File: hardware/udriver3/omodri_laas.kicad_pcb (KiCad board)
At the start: 2 copper layers, 251 parts, among them J1 Conn_01x12, J10 Conn_01x02, J11 Conn_02x04_Odd_Even, J12 Conn_01x07, J13 Conn_01x07, J2 Conn_01x05, J3 Conn_01x03, J4 Conn_01x02, J5 Conn_01x03, J6 Conn_01x03, J7 Conn_01x03, J8 Conn_01x05, J9 Conn_01x05, Q1 CSD88599Q5DC, Q2 CSD88599Q5DC, Q3 CSD88599Q5DC, Q4 CSD88599Q5DC, Q5 CSD88599Q5DC, Q6 CSD88599Q5DC, SW1 B3U-3100P, U1 DRV8353S, U10 TCAN332G, U11 TPS3703, U12 TPS3703, U13 TPD6E05U06, U14 DSLVDS1048, U15 TPD2E001, U16 TPD2E001, U17 TPD2E001, U18 TPD2E001, U19 TPD6E05U06, U2 DRV8353S, U20 DSLVDS1047, U3 MAX17502FxTB, U4 TMS320F28388D, U5 MPM3804GG, U6 MPM3804GG, U7 REF6230, U8 OPA388, U9 TXB0106, X1 ECS-TXO-2016-33-200-TR

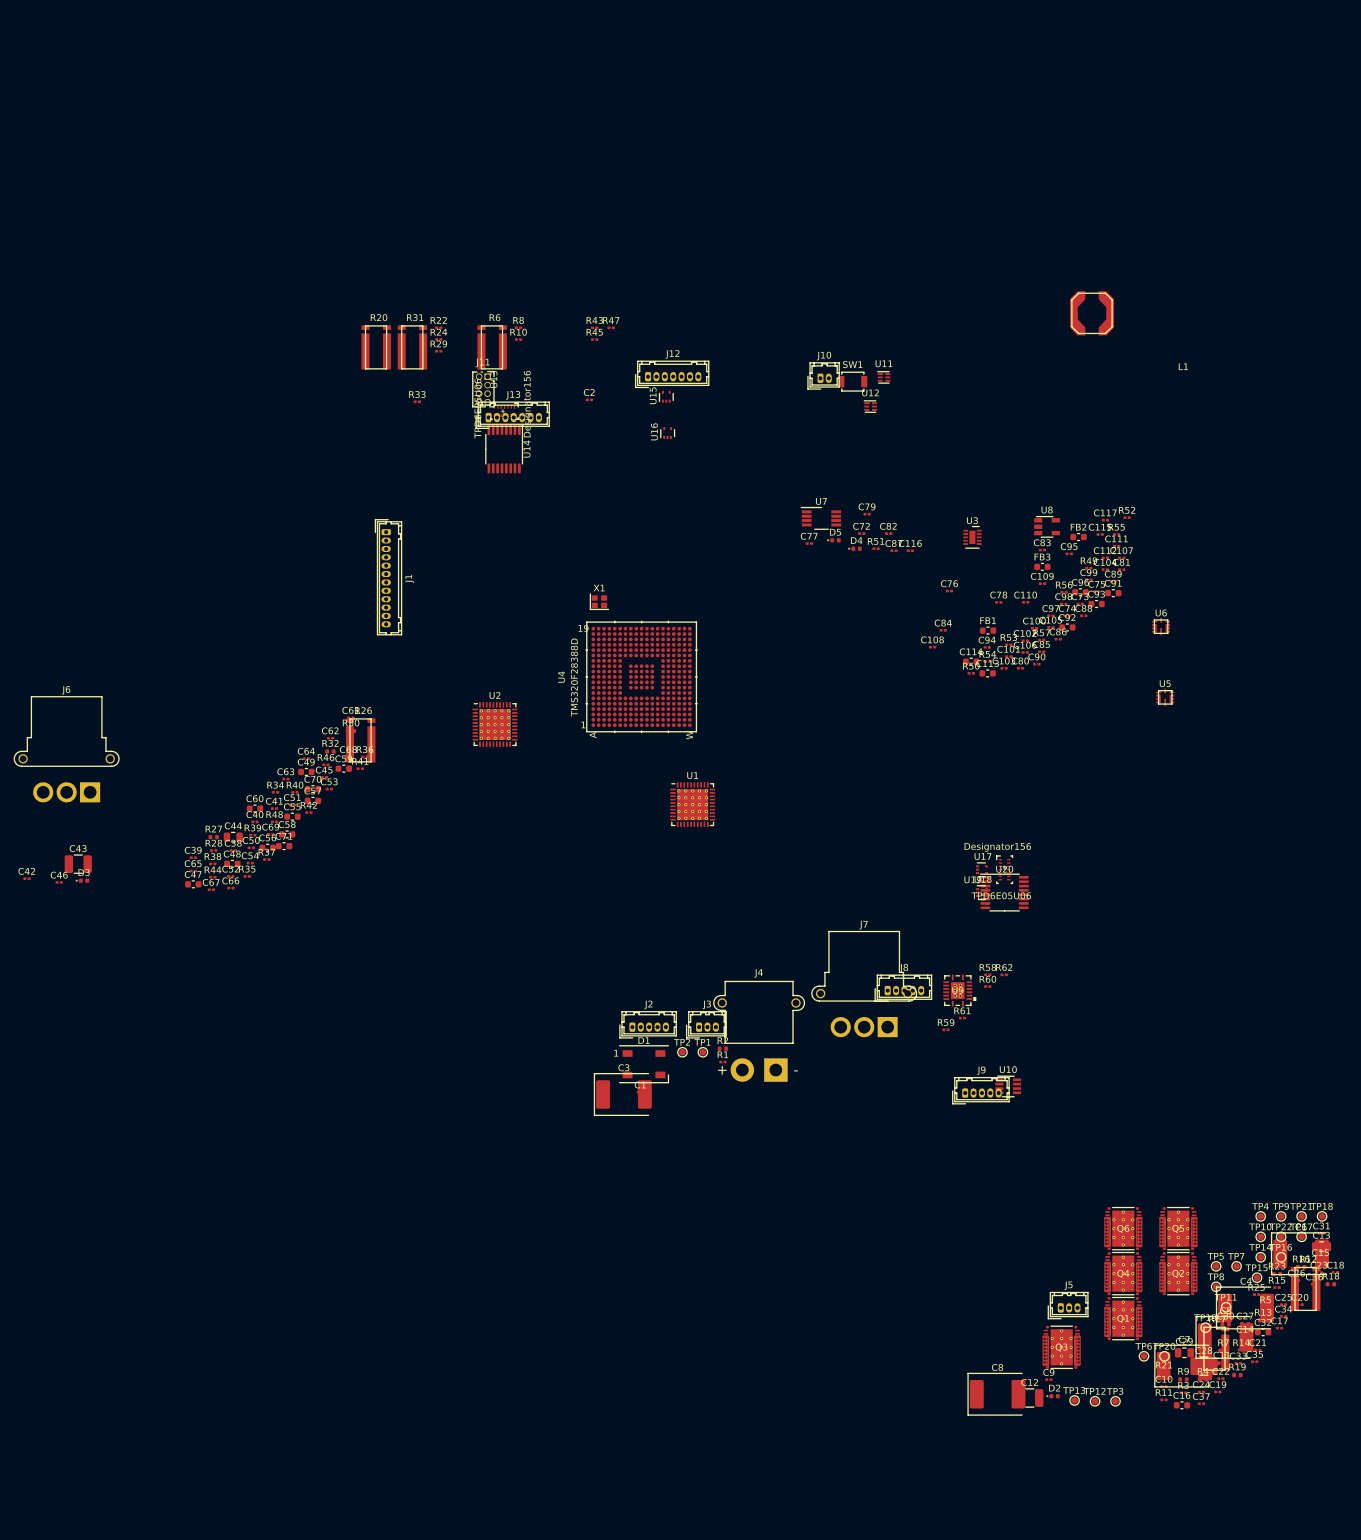
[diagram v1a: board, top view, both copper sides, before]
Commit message: Update of the schematics. Driver and power files split. Placement starting.
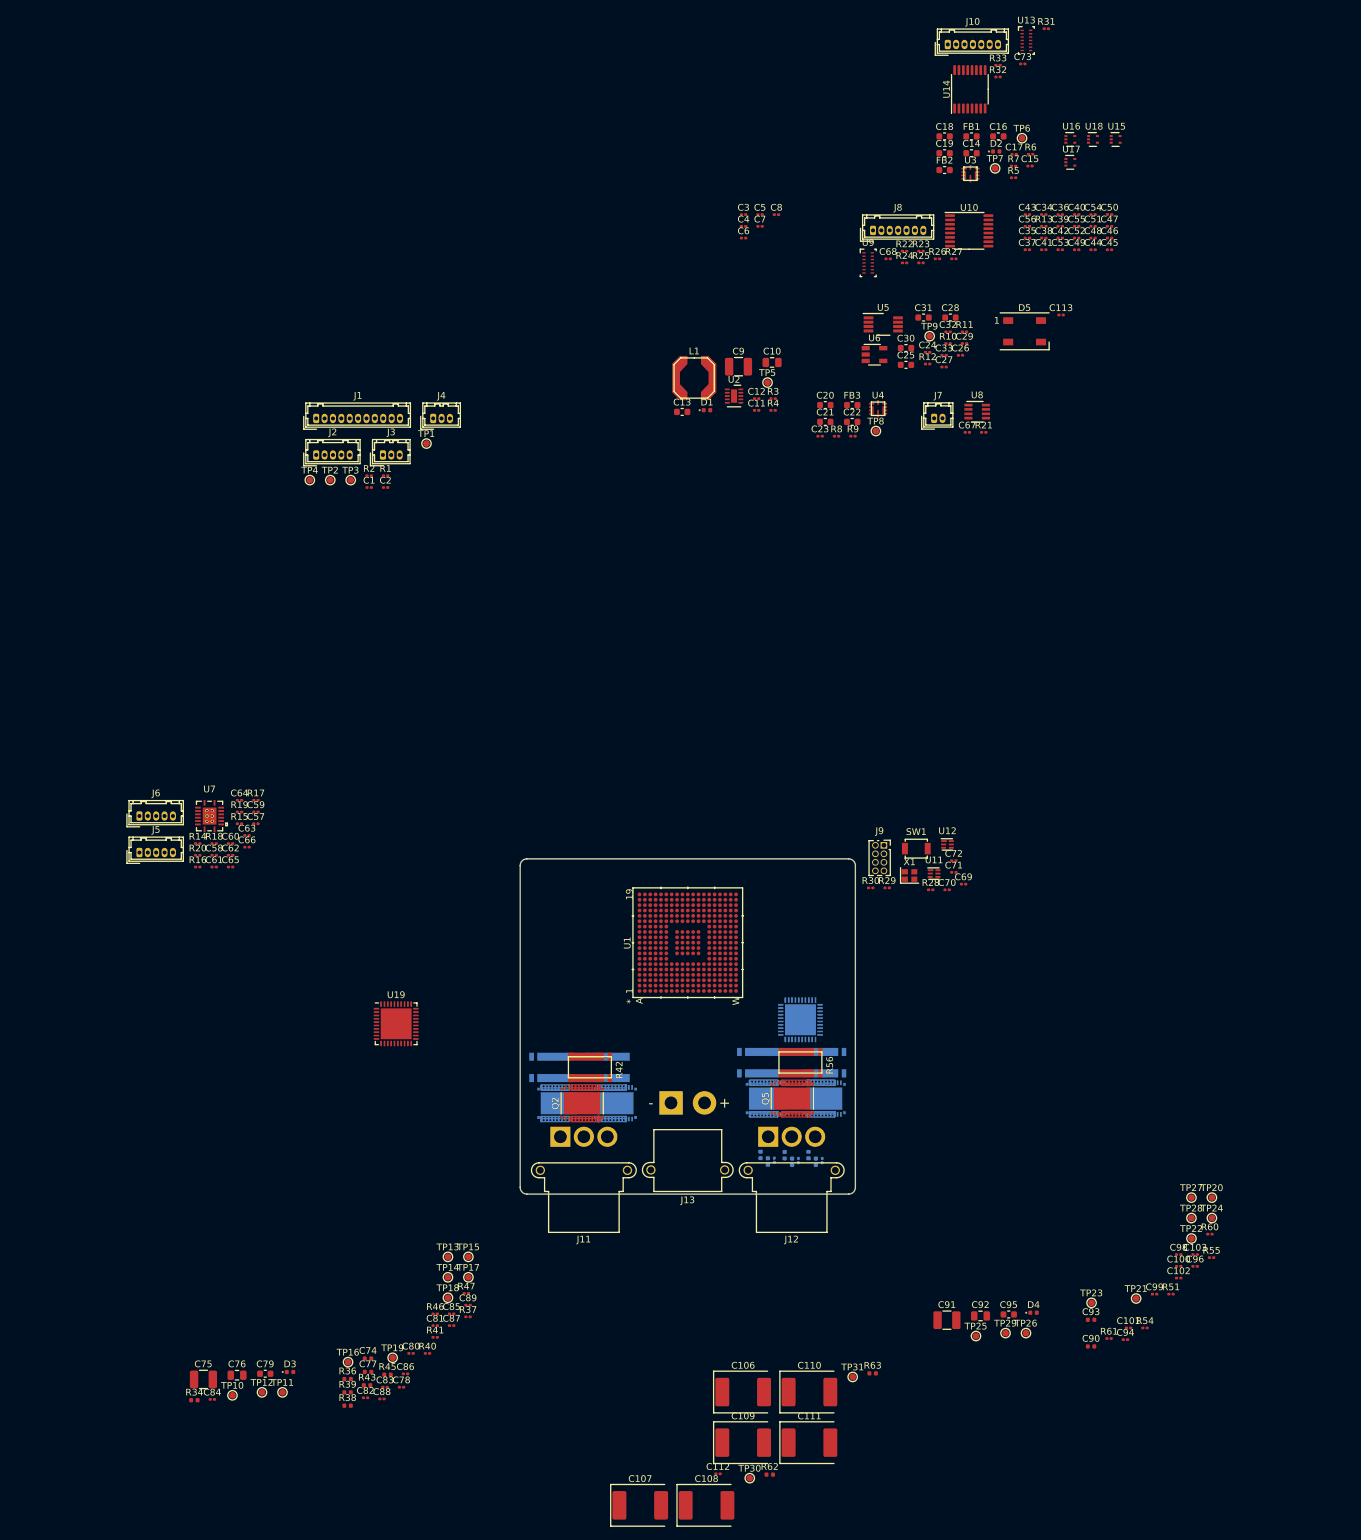
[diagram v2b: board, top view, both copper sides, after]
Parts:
- removed C114: 10uF, Capacitor_SMD:C_0603_1608Metric
- removed C115, C116, C117: 100nF, Capacitor_SMD:C_0201_0603Metric
- added R63: 5.1k, Resistor_SMD:R_0402_1005Metric, F.Cu at (152.6, 126.7)
- added TP23: TestPoint, TestPoint:TestPoint_Pad_D1.0mm, F.Cu at (185.2, 116.2)
- added TP24: TestPoint, TestPoint:TestPoint_Pad_D1.0mm, F.Cu at (203.2, 103.6)
- added TP25: TestPoint, TestPoint:TestPoint_Pad_D1.0mm, F.Cu at (168.0, 121.2)
- added TP26: TestPoint, TestPoint:TestPoint_Pad_D1.0mm, F.Cu at (175.4, 120.7)
- added TP27: TestPoint, TestPoint:TestPoint_Pad_D1.0mm, F.Cu at (200.1, 100.5)
- added TP28: TestPoint, TestPoint:TestPoint_Pad_D1.0mm, F.Cu at (200.1, 103.6)
- added TP29: TestPoint, TestPoint:TestPoint_Pad_D1.0mm, F.Cu at (172.4, 120.7)
- added TP30: TestPoint, TestPoint:TestPoint_Pad_D1.0mm, F.Cu at (134.2, 142.4)
- added TP31: TestPoint, TestPoint:TestPoint_Pad_D1.0mm, F.Cu at (149.6, 127.3)
- C1, C101, C112, C81, C83, C84, C85: value 100nF -> 10nF
- C10: value 10nF -> 100nF; footprint Capacitor_SMD:C_0201_0603Metric -> Capacitor_SMD:C_0805_2012Metric
- C100, C88, C89: value 1uF -> 10nF
- C102, C63, C64, C65, C80, C86: value 100nF -> 1nF
- C104, C105, C97: value 1nF -> 10nF; moved to B.Cu
- C106: value 1uF -> 100uF; footprint Capacitor_SMD:C_0201_0603Metric -> Capacitor_Tantalum_SMD:CP_EIA-7360-38_Kemet-E
- C107, C108, C109, C111: value 100nF -> 100uF; footprint Capacitor_SMD:C_0201_0603Metric -> Capacitor_Tantalum_SMD:CP_EIA-7360-38_Kemet-E
- C11: value 1uF -> 10nF; footprint Capacitor_SMD:C_0402_1005Metric -> Capacitor_SMD:C_0201_0603Metric
- C110: value 10nF -> 100uF; footprint Capacitor_SMD:C_0201_0603Metric -> Capacitor_Tantalum_SMD:CP_EIA-7360-38_Kemet-E
- C113, C47, C48, C49, C55, C56, C70: value 10uF -> 100nF; footprint Capacitor_SMD:C_0603_1608Metric -> Capacitor_SMD:C_0201_0603Metric
- C12: value 10uF -> 1uF; footprint Capacitor_SMD:C_1210_3225Metric -> Capacitor_SMD:C_0201_0603Metric
- C13: value 100nF -> 22uF; footprint Capacitor_SMD:C_0805_2012Metric -> Capacitor_SMD:C_0603_1608Metric
- C14, C30: value 1uF -> 10uF; footprint Capacitor_SMD:C_0402_1005Metric -> Capacitor_SMD:C_0603_1608Metric
- C16: value 47nF -> 10uF
- C17, C23: value 1nF -> 1uF
- C18, C20, C22: value 10nF -> 10uF; footprint Capacitor_SMD:C_0201_0603Metric -> Capacitor_SMD:C_0603_1608Metric
- C19: value 100nF -> 22uF; footprint Capacitor_SMD:C_0201_0603Metric -> Capacitor_SMD:C_0603_1608Metric
- C21: value 10nF -> 22uF; footprint Capacitor_SMD:C_0201_0603Metric -> Capacitor_SMD:C_0603_1608Metric
- C24, C26, C34, C36, C37, C38, C40, C42, C45: value 10nF -> 100nF
- C25: value 1nF -> 10uF; footprint Capacitor_SMD:C_0201_0603Metric -> Capacitor_SMD:C_0603_1608Metric
- C27: footprint Capacitor_SMD:C_0402_1005Metric -> Capacitor_SMD:C_0201_0603Metric
- C28: footprint Capacitor_SMD:C_1210_3225Metric -> Capacitor_SMD:C_0603_1608Metric
- C29: value 100nF -> 1uF; footprint Capacitor_SMD:C_0805_2012Metric -> Capacitor_SMD:C_0201_0603Metric
- C3, C4, C5, C6, C7, C8: value 100uF -> 100nF; footprint Capacitor_Tantalum_SMD:CP_EIA-7360-38_Kemet-E -> Capacitor_SMD:C_0201_0603Metric
- C31: value 1uF -> 10uF; footprint Capacitor_SMD:C_0201_0603Metric -> Capacitor_SMD:C_0603_1608Metric
- C32: value 47nF -> 100nF; footprint Capacitor_SMD:C_0603_1608Metric -> Capacitor_SMD:C_0201_0603Metric
- C33, C39, C41, C98: value 1nF -> 100nF
- C43: value 10uF -> 100nF; footprint Capacitor_SMD:C_1210_3225Metric -> Capacitor_SMD:C_0201_0603Metric
- C44: footprint Capacitor_SMD:C_0805_2012Metric -> Capacitor_SMD:C_0201_0603Metric
- C46, C51, C53, C67, C68, C69: value 1uF -> 100nF
- C57, C58, C59, C96: value 10uF -> 1nF; footprint Capacitor_SMD:C_0603_1608Metric -> Capacitor_SMD:C_0201_0603Metric
- C60: value 10uF -> 1uF; footprint Capacitor_SMD:C_0603_1608Metric -> Capacitor_SMD:C_0201_0603Metric
- C66, C78, C94: value 100nF -> 1uF
- C71: value 10uF -> 10nF; footprint Capacitor_SMD:C_0603_1608Metric -> Capacitor_SMD:C_0201_0603Metric
- C74, C77: value 100nF -> 1uF; footprint Capacitor_SMD:C_0201_0603Metric -> Capacitor_SMD:C_0402_1005Metric
- C75: value 100nF -> 10uF; footprint Capacitor_SMD:C_0201_0603Metric -> Capacitor_SMD:C_1210_3225Metric
- C76: footprint Capacitor_SMD:C_0201_0603Metric -> Capacitor_SMD:C_0805_2012Metric
- C79: value 100nF -> 47nF; footprint Capacitor_SMD:C_0201_0603Metric -> Capacitor_SMD:C_0603_1608Metric
- C87: value 1uF -> 1nF
- C9: value 10nF -> 10uF; footprint Capacitor_SMD:C_0201_0603Metric -> Capacitor_SMD:C_1210_3225Metric
- C90: footprint Capacitor_SMD:C_0201_0603Metric -> Capacitor_SMD:C_0402_1005Metric
- C91: footprint Capacitor_SMD:C_0603_1608Metric -> Capacitor_SMD:C_1210_3225Metric
- C92: value 10uF -> 100nF; footprint Capacitor_SMD:C_0603_1608Metric -> Capacitor_SMD:C_0805_2012Metric
- C93: value 10uF -> 1uF; footprint Capacitor_SMD:C_0603_1608Metric -> Capacitor_SMD:C_0402_1005Metric
- C95: value 1uF -> 47nF; footprint Capacitor_SMD:C_0201_0603Metric -> Capacitor_SMD:C_0603_1608Metric
- C99: value 1nF -> 10nF
- D1: value WS2812B -> LED GREEN; footprint LED_SMD:LED_WS2812B_PLCC4_5.0x5.0mm_P3.2mm -> LED_SMD:LED_0402_1005Metric
- D2: value LED RED -> LED GREEN
- D4: value LED GREEN -> LED RED
- D5: value LED GREEN -> WS2812B; footprint LED_SMD:LED_0402_1005Metric -> LED_SMD:LED_WS2812B_PLCC4_5.0x5.0mm_P3.2mm
- FB1, FB2, FB3: value Ferrite_Bead_Small -> 220R@100MHz
- J1: value Conn_01x12 -> Conn_01x11; footprint Connector_Hirose:Hirose_DF13-12P-1.25DSA_1x12_P1.25mm_Vertical -> Connector_Hirose:Hirose_DF13-11P-1.25DSA_1x11_P1.25mm_Vertical
- J10: value Conn_01x02 -> Conn_01x07; footprint Connector_Hirose:Hirose_DF13-02P-1.25DSA_1x02_P1.25mm_Vertical -> Connector_Hirose:Hirose_DF13-07P-1.25DSA_1x07_P1.25mm_Vertical
- J11: value Conn_02x04_Odd_Even -> Conn_01x03; footprint Connector_PinSocket_1.27mm:PinSocket_2x04_P1.27mm_Vertical -> Connector_AMASS:AMASS_MR30PW-FB_1x03_P3.50mm_Horizontal
- J12: value Conn_01x07 -> Conn_01x03; footprint Connector_Hirose:Hirose_DF13-07P-1.25DSA_1x07_P1.25mm_Vertical -> Connector_AMASS:AMASS_MR30PW-FB_1x03_P3.50mm_Horizontal
- J13: value Conn_01x07 -> Conn_01x02; footprint Connector_Hirose:Hirose_DF13-07P-1.25DSA_1x07_P1.25mm_Vertical -> Connector_AMASS:AMASS_XT30PW-M_1x02_P2.50mm_Horizontal
- J4: value Conn_01x02 -> Conn_01x03; footprint Connector_AMASS:AMASS_XT30PW-M_1x02_P2.50mm_Horizontal -> Connector_Hirose:Hirose_DF13-03P-1.25DSA_1x03_P1.25mm_Vertical
- J5: value Conn_01x03 -> Conn_01x05; footprint Connector_Hirose:Hirose_DF13-03P-1.25DSA_1x03_P1.25mm_Vertical -> Connector_Hirose:Hirose_DF13-05P-1.25DSA_1x05_P1.25mm_Vertical
- J6: value Conn_01x03 -> Conn_01x05; footprint Connector_AMASS:AMASS_MR30PW-FB_1x03_P3.50mm_Horizontal -> Connector_Hirose:Hirose_DF13-05P-1.25DSA_1x05_P1.25mm_Vertical
- J7: value Conn_01x03 -> Conn_01x02; footprint Connector_AMASS:AMASS_MR30PW-FB_1x03_P3.50mm_Horizontal -> Connector_Hirose:Hirose_DF13-02P-1.25DSA_1x02_P1.25mm_Vertical
- J8: value Conn_01x05 -> Conn_01x07; footprint Connector_Hirose:Hirose_DF13-05P-1.25DSA_1x05_P1.25mm_Vertical -> Connector_Hirose:Hirose_DF13-07P-1.25DSA_1x07_P1.25mm_Vertical
- J9: value Conn_01x05 -> Conn_02x04_Odd_Even; footprint Connector_Hirose:Hirose_DF13-05P-1.25DSA_1x05_P1.25mm_Vertical -> Connector_PinSocket_1.27mm:PinSocket_2x04_P1.27mm_Vertical
- L1: footprint udrive3:L_coilcraft_LPS62xx -> udriver3:L_coilcraft_LPS62xx
- Q1, Q3, Q4, Q6: footprint udrive3:VSON_CLIP_22 -> udriver3:VSON_CLIP_22; moved to B.Cu
- Q2, Q5: footprint udrive3:VSON_CLIP_22 -> udriver3:VSON_CLIP_22
- R10, R11: value 120 -> 0.1
- R12: value 0.005 -> 0.1; footprint udrive3:FC4L64 -> Resistor_SMD:R_0201_0603Metric
- R13: value 5.1k -> 56; footprint Resistor_SMD:R_0402_1005Metric -> Resistor_SMD:R_0201_0603Metric
- R14: value 220 -> 1k
- R15: value 10k -> 1k
- R16, R19, R30: value 100k -> 1k; footprint Resistor_SMD:R_0402_1005Metric -> Resistor_SMD:R_0201_0603Metric
- R17, R20: value 0.005 -> 1k; footprint udrive3:FC4L64 -> Resistor_SMD:R_0201_0603Metric
- R18, R4: value 5.1k -> 1k; footprint Resistor_SMD:R_0402_1005Metric -> Resistor_SMD:R_0201_0603Metric
- R2: value 100k -> 120; footprint Resistor_SMD:R_0402_1005Metric -> Resistor_SMD:R_0201_0603Metric
- R21: value 5.1k -> 120; footprint Resistor_SMD:R_0402_1005Metric -> Resistor_SMD:R_0201_0603Metric
- R22, R24: value 120 -> 100
- R23: value 100k -> 100; footprint Resistor_SMD:R_0402_1005Metric -> Resistor_SMD:R_0201_0603Metric
- R25: value 120 -> 10k
- R26, R31: value 0.005 -> 10k; footprint udrive3:FC4L64 -> Resistor_SMD:R_0201_0603Metric
- R27, R32: value 5.1k -> 10k; footprint Resistor_SMD:R_0402_1005Metric -> Resistor_SMD:R_0201_0603Metric
- R28: value 220 -> 10k
- R3, R8: value 120 -> 100k
- R34: value 470 -> 100k; footprint Resistor_SMD:R_0201_0603Metric -> Resistor_SMD:R_0402_1005Metric
- R35: value 100k -> 0.005; footprint Resistor_SMD:R_0201_0603Metric -> udriver3:FC4L64; moved to B.Cu
- R36: value 22.1k -> 5.1k; footprint Resistor_SMD:R_0201_0603Metric -> Resistor_SMD:R_0402_1005Metric
- R37: value 220 -> 120
- R38, R39: footprint Resistor_SMD:R_0201_0603Metric -> Resistor_SMD:R_0402_1005Metric
- R40: value 56 -> 120
- R41, R51: value 1k -> 120
- R42: value 1k -> 0.005; footprint Resistor_SMD:R_0201_0603Metric -> udriver3:FC4L64
- R43, R45: value 1k -> 5.1k; footprint Resistor_SMD:R_0201_0603Metric -> Resistor_SMD:R_0402_1005Metric
- R44: value 1k -> 0.005; footprint Resistor_SMD:R_0201_0603Metric -> udriver3:FC4L64; moved to B.Cu
- R46: value 1k -> 470
- R47: value 1k -> 10k
- R48: value 120 -> 100k; footprint Resistor_SMD:R_0201_0603Metric -> Resistor_SMD:R_0402_1005Metric; moved to B.Cu
- R49: value 10k -> 0.005; footprint Resistor_SMD:R_0201_0603Metric -> udriver3:FC4L64; moved to B.Cu
- R5, R9: footprint Resistor_SMD:R_0402_1005Metric -> Resistor_SMD:R_0201_0603Metric
- R50, R57: value 10k -> 5.1k; footprint Resistor_SMD:R_0201_0603Metric -> Resistor_SMD:R_0402_1005Metric; moved to B.Cu
- R52, R53: value 100 -> 100k; footprint Resistor_SMD:R_0201_0603Metric -> Resistor_SMD:R_0402_1005Metric; moved to B.Cu
- R54: value 100 -> 120
- R55: value 10k -> 120
- R56: value 10k -> 0.005; footprint Resistor_SMD:R_0201_0603Metric -> udriver3:FC4L64
- R58: value 0.1 -> 0.005; footprint Resistor_SMD:R_0201_0603Metric -> udriver3:FC4L64; moved to B.Cu
- R59: value 0.1 -> 5.1k; footprint Resistor_SMD:R_0201_0603Metric -> Resistor_SMD:R_0402_1005Metric; moved to B.Cu
- R6: value 0.005 -> 22.1k; footprint udrive3:FC4L64 -> Resistor_SMD:R_0201_0603Metric
- R60: value 10k -> 470
- R62: value 10k -> 100k; footprint Resistor_SMD:R_0201_0603Metric -> Resistor_SMD:R_0402_1005Metric
- R7: value 5.1k -> 470; footprint Resistor_SMD:R_0402_1005Metric -> Resistor_SMD:R_0201_0603Metric
- U1: value DRV8353S -> TMS320F28388D; footprint Package_DFN_QFN:QFN-40-1EP_6x6mm_P0.5mm_EP4.6x4.6mm_ThermalVias -> udriver3:NFBGA_337
- U10: value TCAN332G -> DSLVDS1048; footprint Package_TO_SOT_SMD:TSOT-23-8 -> Package_SO:TSSOP-16_4.4x5mm_P0.65mm
- U13: footprint udrive3:USON_14 -> udriver3:USON_14
- U14: value DSLVDS1048 -> DSLVDS1047
- U19: value TPD6E05U06 -> DRV8353S; footprint udrive3:USON_14 -> Package_DFN_QFN:QFN-40-1EP_6x6mm_P0.5mm_EP4.6x4.6mm
- U2: value DRV8353S -> MAX17502FxTB; footprint Package_DFN_QFN:QFN-40-1EP_6x6mm_P0.5mm_EP4.6x4.6mm_ThermalVias -> Package_DFN_QFN:TDFN-10-1EP_2x3mm_P0.5mm_EP0.9x2mm
- U20: value DSLVDS1047 -> DRV8353S; footprint Package_SO:TSSOP-16_4.4x5mm_P0.65mm -> Package_DFN_QFN:QFN-40-1EP_6x6mm_P0.5mm_EP4.6x4.6mm; moved to B.Cu
- U3: value MAX17502FxTB -> MPM3804GG; footprint Package_DFN_QFN:TDFN-10-1EP_2x3mm_P0.5mm_EP0.9x2mm -> udriver3:QFN-10_2x2mm_P0.5mm
- U4: value TMS320F28388D -> MPM3804GG; footprint udrive3:NFBGA_337 -> udriver3:QFN-10_2x2mm_P0.5mm
- U5: value MPM3804GG -> REF6230; footprint udrive3:QFN-10_2x2mm_P0.5mm -> Package_SO:VSSOP-8_3.0x3.0mm_P0.65mm
- U6: value MPM3804GG -> OPA388; footprint udrive3:QFN-10_2x2mm_P0.5mm -> Package_TO_SOT_SMD:TSOT-23-5
- U7: value REF6230 -> TXB0106; footprint Package_SO:VSSOP-8_3.0x3.0mm_P0.65mm -> udriver3:PVQFN_17
- U8: value OPA388 -> TCAN332G; footprint Package_TO_SOT_SMD:TSOT-23-5 -> Package_TO_SOT_SMD:TSOT-23-8
- U9: value TXB0106 -> TPD6E05U06; footprint udrive3:PVQFN_17 -> udriver3:USON_14
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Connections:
- C1 pad 1: VDD_3V3 -> /sheet5F597565/ANALOG_IN2
- C10 pad 1: /F2838x GPIOs/ANALOG_IN1 -> VPOWER
- C100 pad 1: 5V0 -> /sheet5F597565/M2_Ib
- C101 pad 1: VDD_3V3 -> /sheet5F597565/M2_Ia
- C102 pad 1: 5V0 -> /Sheet5F71C92D/SPB
- C102 pad 2: GND -> /Sheet5F71C92D/SNB
- C103 pad 1: /Quadrature Encoders for motor 1 & 2/ENC2_A -> /Sheet5F71C92D/SPC
- C103 pad 2: GND -> /Sheet5F71C92D/SNC
- C104 pad 1: /Quadrature Encoders for motor 1 & 2/ENC2_B -> /sheet5F597565/M2_Vb
- C105 pad 1: /Quadrature Encoders for motor 1 & 2/ENC2_I -> /sheet5F597565/M2_Vc
- C106 pad 1: 5V0 -> VPOWER
- C106 pad 2: GND -> Net-(C106-Pad2)
- C107 pad 1: VDD_3V3 -> VPOWER
- C107 pad 2: GND -> Net-(C107-Pad2)
- C108 pad 1: VDD_3V3 -> VPOWER
- C108 pad 2: GND -> Net-(C108-Pad2)
- C109 pad 1: VDD_3V3 -> Net-(C106-Pad2)
- C11 pad 1: VPOWER -> Net-(C11-Pad1)
- C11 pad 2: Net-(C11-Pad2) -> GND
- C110 pad 1: /JTAG Bus + Oscillator + Reset/~XRSn~ -> Net-(C107-Pad2)
- C111 pad 1: VDD_3V3 -> Net-(C108-Pad2)
- C112 pad 1: VDD_3V3 -> /sheet5F597565/M1_Vbus
- C113 pad 1: Net-(C113-Pad1) -> VDD_3V3
- C12 pad 1: VPOWER -> Net-(C12-Pad1)
- C13 pad 1: VPOWER -> 5V0
- C14 pad 1: GND -> VDD_3V3
- C14 pad 2: /DRV driver for motor2/VGLS -> GND
- C15 pad 1: /DRV driver for motor2/DVDD -> VDD_3V3
- C16 pad 1: Net-(C16-Pad1) -> VDDA_3V3
- C16 pad 2: Net-(C16-Pad2) -> GND
- C17 pad 1: /DRV driver for motor2/SPA -> VDDA_3V3
- C17 pad 2: /DRV driver for motor2/SNA -> GND
- C18 pad 1: /F2838x GPIOs/M2_Va -> 5V0
- C19 pad 1: REF_3V0_BUF -> /Power distribution/Sheet5F5BE68A/3V3
- C2 pad 1: /F2838x GPIOs/ANALOG_IN2 -> /sheet5F597565/ANALOG_IN1
- C20 pad 1: /F2838x GPIOs/M2_Ic -> 5V0
- C21 pad 1: /F2838x GPIOs/M2_Ib -> /Power distribution/Sheet5F5BF411/1V2
- C22 pad 1: /F2838x GPIOs/M2_Ia -> VDD_1V2
- C23 pad 1: /DRV driver for motor2/SPB -> VDD_1V2
- C23 pad 2: /DRV driver for motor2/SNB -> GND
- C24 pad 1: /F2838x GPIOs/M2_Vb -> VDDA_3V3
- C25 pad 1: /DRV driver for motor2/SPC -> VDDA_3V3
- C25 pad 2: /DRV driver for motor2/SNC -> GND
- C26 pad 1: /F2838x GPIOs/M2_Vc -> VDDA_3V3
- C27 pad 1: VPOWER -> Net-(C27-Pad1)
- C27 pad 2: Net-(C27-Pad2) -> GND
- C28 pad 1: VPOWER -> Net-(C28-Pad1)
- C29 pad 1: VPOWER -> /Power distribution/Sheet5F5C0182/REF_3V0
- C3 pad 1: VPOWER -> VDDA_3V3
- C3 pad 2: Net-(C3-Pad2) -> GND
- C30 pad 1: GND -> Net-(C30-Pad1)
- C30 pad 2: /DRV driver for motor1/VGLS -> GND
- C31 pad 1: /DRV driver for motor1/DVDD -> Net-(C31-Pad1)
- C32 pad 1: Net-(C32-Pad1) -> REF_3V0_BUF
- C32 pad 2: Net-(C32-Pad2) -> GND
- C33 pad 1: /DRV driver for motor1/SPA -> REF_3V0_BUF
- C33 pad 2: /DRV driver for motor1/SNA -> GND
- C34 pad 1: /F2838x GPIOs/M1_Va -> VDD_1V2
- C35 pad 1: REF_3V0_BUF -> VDD_1V2
- C36 pad 1: /F2838x GPIOs/M1_Ic -> VDD_1V2
- C37 pad 1: /F2838x GPIOs/M1_Ib -> VDD_1V2
- C38 pad 1: /F2838x GPIOs/M1_Ia -> VDD_1V2
- C39 pad 1: /DRV driver for motor1/SPB -> VDD_1V2
- C39 pad 2: /DRV driver for motor1/SNB -> GND
- C4 pad 1: VPOWER -> VDDA_3V3
- C4 pad 2: Net-(C4-Pad2) -> GND
- C40 pad 1: /F2838x GPIOs/M1_Vb -> VDD_1V2
- C41 pad 1: /DRV driver for motor1/SPC -> VDD_3V3
- C41 pad 2: /DRV driver for motor1/SNC -> GND
- C42 pad 1: /F2838x GPIOs/M1_Vc -> VDD_3V3
- C43 pad 1: VPOWER -> VDD_3V3
- C44 pad 1: VPOWER -> VDD_3V3
- C45 pad 1: Net-(C45-Pad1) -> VDD_3V3
- C46 pad 1: Net-(C46-Pad1) -> VDD_3V3
- C47 pad 1: 5V0 -> VDD_3V3
- C48 pad 1: 5V0 -> VDD_3V3
- C49 pad 1: VDDA_3V3 -> VDD_3V3
- C5 pad 1: VPOWER -> VDD_3V3
- C5 pad 2: Net-(C5-Pad2) -> GND
- C50 pad 1: VDDA_3V3 -> VDD_3V3
- C55 pad 1: 5V0 -> VDD_3V3
- C56 pad 1: /Power distribution/3V3 -> VDD_3V3
- C57 pad 1: /Power distribution/3V3 -> /sheet5F5A100E/ENC1_A
- C58 pad 1: 5V0 -> /sheet5F5A100E/ENC1_B
- C59 pad 1: /Power distribution/1V2 -> /sheet5F5A100E/ENC1_I
- C6 pad 1: Net-(C3-Pad2) -> VDD_3V3
- C60 pad 1: /Power distribution/1V2 -> 5V0
- C61 pad 1: VDD_1V2 -> VDD_3V3
- C62 pad 1: VDD_1V2 -> 5V0
- C63 pad 1: VDD_1V2 -> /sheet5F5A100E/ENC2_A
- C64 pad 1: VDD_1V2 -> /sheet5F5A100E/ENC2_B
- C65 pad 1: VDD_1V2 -> /sheet5F5A100E/ENC2_I
- C66 pad 1: VDD_1V2 -> 5V0
- C67 pad 1: VDD_1V2 -> VDD_3V3
- C68 pad 1: VDD_1V2 -> VDD_3V3
- C69 pad 1: VDD_1V2 -> VDD_3V3
- C7 pad 1: Net-(C4-Pad2) -> VDD_3V3
- C70 pad 1: VDD_1V2 -> VDD_3V3
- C71 pad 1: VDD_1V2 -> /JTAG + CLOCK + RESET/~XRSn~
- C74 pad 1: VDD_3V3 -> VPOWER
- C74 pad 2: GND -> Net-(C74-Pad2)
- C75 pad 1: VDD_3V3 -> VPOWER
- C76 pad 1: VDD_3V3 -> VPOWER
- C77 pad 1: VDD_3V3 -> GND
- C77 pad 2: GND -> /Sheet5F71C5AE/VGLS
- C78 pad 1: VDD_3V3 -> /Sheet5F71C5AE/DVDD
- C79 pad 1: VDD_3V3 -> Net-(C79-Pad1)
- C79 pad 2: GND -> Net-(C79-Pad2)
- C8 pad 1: Net-(C5-Pad2) -> VDD_3V3
- C80 pad 1: VDD_3V3 -> /Sheet5F71C5AE/SPA
- C80 pad 2: GND -> /Sheet5F71C5AE/SNA
- C81 pad 1: VDD_3V3 -> /sheet5F597565/M1_Va
- C82 pad 1: VDD_3V3 -> REF_3V0_BUF
- C83 pad 1: VDD_3V3 -> /sheet5F597565/M1_Ic
- C84 pad 1: VDDA_3V3 -> /sheet5F597565/M1_Ib
- C85 pad 1: VDD_3V3 -> /sheet5F597565/M1_Ia
- C86 pad 1: VDD_3V3 -> /Sheet5F71C5AE/SPB
- C86 pad 2: GND -> /Sheet5F71C5AE/SNB
- C87 pad 1: VDD_3V3 -> /Sheet5F71C5AE/SPC
- C87 pad 2: GND -> /Sheet5F71C5AE/SNC
- C88 pad 1: VDD_3V3 -> /sheet5F597565/M1_Vb
- C89 pad 1: VDD_3V3 -> /sheet5F597565/M1_Vc
- C9 pad 1: /F2838x GPIOs/M1_Vbus -> VPOWER
- C90 pad 1: VDD_3V3 -> VPOWER
- C90 pad 2: GND -> Net-(C90-Pad2)
- C91 pad 1: VDD_3V3 -> VPOWER
- C92 pad 1: VDD_3V3 -> VPOWER
- C93 pad 1: VDDA_3V3 -> GND
- C93 pad 2: GND -> /Sheet5F71C92D/VGLS
- C94 pad 1: VDDA_3V3 -> /Sheet5F71C92D/DVDD
- C95 pad 2: GND -> Net-(C95-Pad2)
- C96 pad 1: /Power distribution/REF_3V0 -> /Sheet5F71C92D/SPA
- C96 pad 2: GND -> /Sheet5F71C92D/SNA
- C97 pad 1: /Quadrature Encoders for motor 1 & 2/ENC1_A -> /sheet5F597565/M2_Va
- C98 pad 1: /Quadrature Encoders for motor 1 & 2/ENC1_B -> REF_3V0_BUF
- C99 pad 1: /Quadrature Encoders for motor 1 & 2/ENC1_I -> /sheet5F597565/M2_Ic
- D1 pad 1: VDD_3V3 -> Net-(D1-Pad1)
- D1 pad 2: Net-(D1-Pad2) -> 5V0
- D2 pad 2: VDD_3V3 -> /Power distribution/Sheet5F5BE68A/3V3
- D4 pad 2: 5V0 -> VDD_3V3
- D5 pad 1: Net-(D5-Pad1) -> VDD_3V3
- D5 pad 2: /Power distribution/3V3 -> Net-(D5-Pad2)
- FB1 pad 2: /Power distribution/3V3 -> /Power distribution/Sheet5F5BE68A/3V3
- FB2 pad 2: /Power distribution/3V3 -> /Power distribution/Sheet5F5BE68A/3V3
- FB3 pad 2: /Power distribution/1V2 -> /Power distribution/Sheet5F5BF411/1V2
- J1 pad 10: /F2838x GPIOs/GPIO3 -> /sheet5F597565/GPIO3
- J1 pad 11: /F2838x GPIOs/GPIO4 -> /sheet5F597565/GPIO4
- J1 pad 3: /F2838x GPIOs/COM_SPI_SOMI -> /sheet5F597565/COM_SPI_SOMI
- J1 pad 4: /F2838x GPIOs/COM_SPI_CLK -> /sheet5F597565/COM_SPI_CLK
- J1 pad 5: /F2838x GPIOs/~COM_SPI_CSn~ -> /sheet5F597565/~COM_SPI_CSn~
- J1 pad 6: /F2838x GPIOs/COM_SPI_SIMO -> /sheet5F597565/COM_SPI_SIMO
- J1 pad 7: /F2838x GPIOs/GPIO0 -> /sheet5F597565/GPIO0
- J1 pad 8: /F2838x GPIOs/GPIO1 -> /sheet5F597565/GPIO1
- J1 pad 9: /F2838x GPIOs/GPIO2 -> /sheet5F597565/GPIO2
- J10 pad 1: /CAN Bus link/CAN_H -> GND
- J10 pad 2: /CAN Bus link/CAN_L -> /sheet5F5DA2E4/TX_CLK_LVDS_N
- J11 pad 1: /JTAG Bus + Oscillator + Reset/~TRSTn~ -> /Sheet5F71C5AE/MOTOR_CH1
- J11 pad 2: VDD_3V3 -> /Sheet5F71C5AE/MOTOR_CH2
- J11 pad 3: /JTAG Bus + Oscillator + Reset/TCK -> /Sheet5F71C5AE/MOTOR_CH3
- J12 pad 1: GND -> /Sheet5F71C92D/MOTOR_CH1
- J12 pad 2: /FSI Rx Bus Link/RX_CLK_LVDS_N -> /Sheet5F71C92D/MOTOR_CH2
- J12 pad 3: /FSI Rx Bus Link/RX_CLK_LVDS_P -> /Sheet5F71C92D/MOTOR_CH3
- J13 pad 1: GND -> VPOWER
- J13 pad 2: /FSI Tx Bus Link/TX_CLK_LVDS_N -> GND
- J2 pad 2: /F2838x GPIOs/SPI_SOMI -> /sheet5F597565/SPI_SOMI
- J2 pad 3: /F2838x GPIOs/SPI_CLK -> /sheet5F597565/SPI_CLK
- J2 pad 4: /F2838x GPIOs/~SPI_CSn~ -> /sheet5F597565/~SPI_CSn~
- J2 pad 5: /F2838x GPIOs/SPI_SIMO -> /sheet5F597565/SPI_SIMO
- J4 pad 1: VPOWER -> GND
- J4 pad 2: GND -> Net-(J4-Pad2)
- J5 pad 1: GND -> /sheet5F5A100E/ENC1_A
- J5 pad 2: Net-(J5-Pad2) -> /sheet5F5A100E/ENC1_B
- J5 pad 3: VDDA_3V3 -> /sheet5F5A100E/ENC1_I
- J6 pad 1: /DRV driver for motor2/MOTOR_CH1 -> /sheet5F5A100E/ENC2_A
- J6 pad 2: /DRV driver for motor2/MOTOR_CH2 -> /sheet5F5A100E/ENC2_B
- J6 pad 3: /DRV driver for motor2/MOTOR_CH3 -> /sheet5F5A100E/ENC2_I
- J7 pad 1: /DRV driver for motor1/MOTOR_CH1 -> /sheet5F5B5755/CAN_H
- J7 pad 2: /DRV driver for motor1/MOTOR_CH2 -> /sheet5F5B5755/CAN_L
- J8 pad 1: /Quadrature Encoders for motor 1 & 2/ENC1_A -> GND
- J8 pad 2: /Quadrature Encoders for motor 1 & 2/ENC1_B -> /sheet5F5B5756/RX_CLK_LVDS_N
- J8 pad 3: /Quadrature Encoders for motor 1 & 2/ENC1_I -> /sheet5F5B5756/RX_CLK_LVDS_P
- J8 pad 4: 5V0 -> /sheet5F5B5756/RX_D0_LVDS_N
- J8 pad 5: GND -> /sheet5F5B5756/RX_D0_LVDS_P
- J9 pad 1: /Quadrature Encoders for motor 1 & 2/ENC2_A -> /JTAG + CLOCK + RESET/~TRSTn~
- J9 pad 2: /Quadrature Encoders for motor 1 & 2/ENC2_B -> VDD_3V3
- J9 pad 3: /Quadrature Encoders for motor 1 & 2/ENC2_I -> /JTAG + CLOCK + RESET/TCK
- J9 pad 4: 5V0 -> GND
- J9 pad 5: GND -> /JTAG + CLOCK + RESET/TMS
- Q1 pad 1: /DRV driver for motor2/GHA -> /Sheet5F71C5AE/GHA
- Q1 pad 10: /DRV driver for motor2/MOTOR_CH1 -> /Sheet5F71C5AE/MOTOR_CH1
- Q1 pad 11: /DRV driver for motor2/MOTOR_CH1 -> /Sheet5F71C5AE/MOTOR_CH1
- Q1 pad 2: /DRV driver for motor2/SHA -> /Sheet5F71C5AE/SHA
- Q1 pad 22: /DRV driver for motor2/GLA -> /Sheet5F71C5AE/GLA
- Q1 pad 3: /DRV driver for motor2/MOTOR_CH1 -> /Sheet5F71C5AE/MOTOR_CH1
- Q1 pad 4: /DRV driver for motor2/MOTOR_CH1 -> /Sheet5F71C5AE/MOTOR_CH1
- Q1 pad 5: /DRV driver for motor2/MOTOR_CH1 -> /Sheet5F71C5AE/MOTOR_CH1
- Q1 pad 6: /DRV driver for motor2/MOTOR_CH1 -> /Sheet5F71C5AE/MOTOR_CH1
- Q1 pad 7: /DRV driver for motor2/MOTOR_CH1 -> /Sheet5F71C5AE/MOTOR_CH1
- Q1 pad 8: /DRV driver for motor2/MOTOR_CH1 -> /Sheet5F71C5AE/MOTOR_CH1
- Q1 pad 9: /DRV driver for motor2/MOTOR_CH1 -> /Sheet5F71C5AE/MOTOR_CH1
- Q2 pad 1: /DRV driver for motor2/GHB -> /Sheet5F71C5AE/GHB
- Q2 pad 10: /DRV driver for motor2/MOTOR_CH2 -> /Sheet5F71C5AE/MOTOR_CH2
- Q2 pad 11: /DRV driver for motor2/MOTOR_CH2 -> /Sheet5F71C5AE/MOTOR_CH2
- Q2 pad 2: /DRV driver for motor2/SHB -> /Sheet5F71C5AE/SHB
- Q2 pad 22: /DRV driver for motor2/GLB -> /Sheet5F71C5AE/GLB
- Q2 pad 3: /DRV driver for motor2/MOTOR_CH2 -> /Sheet5F71C5AE/MOTOR_CH2
- Q2 pad 4: /DRV driver for motor2/MOTOR_CH2 -> /Sheet5F71C5AE/MOTOR_CH2
- Q2 pad 5: /DRV driver for motor2/MOTOR_CH2 -> /Sheet5F71C5AE/MOTOR_CH2
- Q2 pad 6: /DRV driver for motor2/MOTOR_CH2 -> /Sheet5F71C5AE/MOTOR_CH2
- Q2 pad 7: /DRV driver for motor2/MOTOR_CH2 -> /Sheet5F71C5AE/MOTOR_CH2
- Q2 pad 8: /DRV driver for motor2/MOTOR_CH2 -> /Sheet5F71C5AE/MOTOR_CH2
- Q2 pad 9: /DRV driver for motor2/MOTOR_CH2 -> /Sheet5F71C5AE/MOTOR_CH2
- Q3 pad 1: /DRV driver for motor2/GHC -> /Sheet5F71C5AE/GHC
- Q3 pad 10: /DRV driver for motor2/MOTOR_CH3 -> /Sheet5F71C5AE/MOTOR_CH3
- Q3 pad 11: /DRV driver for motor2/MOTOR_CH3 -> /Sheet5F71C5AE/MOTOR_CH3
- Q3 pad 2: /DRV driver for motor2/SHC -> /Sheet5F71C5AE/SHC
- Q3 pad 22: /DRV driver for motor2/GLC -> /Sheet5F71C5AE/GLC
- Q3 pad 3: /DRV driver for motor2/MOTOR_CH3 -> /Sheet5F71C5AE/MOTOR_CH3
- Q3 pad 4: /DRV driver for motor2/MOTOR_CH3 -> /Sheet5F71C5AE/MOTOR_CH3
- Q3 pad 5: /DRV driver for motor2/MOTOR_CH3 -> /Sheet5F71C5AE/MOTOR_CH3
- Q3 pad 6: /DRV driver for motor2/MOTOR_CH3 -> /Sheet5F71C5AE/MOTOR_CH3
- Q3 pad 7: /DRV driver for motor2/MOTOR_CH3 -> /Sheet5F71C5AE/MOTOR_CH3
- Q3 pad 8: /DRV driver for motor2/MOTOR_CH3 -> /Sheet5F71C5AE/MOTOR_CH3
- Q3 pad 9: /DRV driver for motor2/MOTOR_CH3 -> /Sheet5F71C5AE/MOTOR_CH3
- Q4 pad 1: /DRV driver for motor1/GHA -> /Sheet5F71C92D/GHA
- Q4 pad 10: /DRV driver for motor1/MOTOR_CH1 -> /Sheet5F71C92D/MOTOR_CH1
- Q4 pad 11: /DRV driver for motor1/MOTOR_CH1 -> /Sheet5F71C92D/MOTOR_CH1
- Q4 pad 2: /DRV driver for motor1/SHA -> /Sheet5F71C92D/SHA
- Q4 pad 22: /DRV driver for motor1/GLA -> /Sheet5F71C92D/GLA
- Q4 pad 3: /DRV driver for motor1/MOTOR_CH1 -> /Sheet5F71C92D/MOTOR_CH1
- Q4 pad 4: /DRV driver for motor1/MOTOR_CH1 -> /Sheet5F71C92D/MOTOR_CH1
- Q4 pad 5: /DRV driver for motor1/MOTOR_CH1 -> /Sheet5F71C92D/MOTOR_CH1
- Q4 pad 6: /DRV driver for motor1/MOTOR_CH1 -> /Sheet5F71C92D/MOTOR_CH1
- Q4 pad 7: /DRV driver for motor1/MOTOR_CH1 -> /Sheet5F71C92D/MOTOR_CH1
- Q4 pad 8: /DRV driver for motor1/MOTOR_CH1 -> /Sheet5F71C92D/MOTOR_CH1
- Q4 pad 9: /DRV driver for motor1/MOTOR_CH1 -> /Sheet5F71C92D/MOTOR_CH1
- Q5 pad 1: /DRV driver for motor1/GHB -> /Sheet5F71C92D/GHB
- Q5 pad 10: /DRV driver for motor1/MOTOR_CH2 -> /Sheet5F71C92D/MOTOR_CH2
- Q5 pad 11: /DRV driver for motor1/MOTOR_CH2 -> /Sheet5F71C92D/MOTOR_CH2
- Q5 pad 2: /DRV driver for motor1/SHB -> /Sheet5F71C92D/SHB
- Q5 pad 22: /DRV driver for motor1/GLB -> /Sheet5F71C92D/GLB
- Q5 pad 3: /DRV driver for motor1/MOTOR_CH2 -> /Sheet5F71C92D/MOTOR_CH2
- Q5 pad 4: /DRV driver for motor1/MOTOR_CH2 -> /Sheet5F71C92D/MOTOR_CH2
- Q5 pad 5: /DRV driver for motor1/MOTOR_CH2 -> /Sheet5F71C92D/MOTOR_CH2
- Q5 pad 6: /DRV driver for motor1/MOTOR_CH2 -> /Sheet5F71C92D/MOTOR_CH2
- Q5 pad 7: /DRV driver for motor1/MOTOR_CH2 -> /Sheet5F71C92D/MOTOR_CH2
- Q5 pad 8: /DRV driver for motor1/MOTOR_CH2 -> /Sheet5F71C92D/MOTOR_CH2
- Q5 pad 9: /DRV driver for motor1/MOTOR_CH2 -> /Sheet5F71C92D/MOTOR_CH2
- Q6 pad 1: /DRV driver for motor1/GHC -> /Sheet5F71C92D/GHC
- Q6 pad 10: /DRV driver for motor1/MOTOR_CH3 -> /Sheet5F71C92D/MOTOR_CH3
- Q6 pad 11: /DRV driver for motor1/MOTOR_CH3 -> /Sheet5F71C92D/MOTOR_CH3
- Q6 pad 2: /DRV driver for motor1/SHC -> /Sheet5F71C92D/SHC
- Q6 pad 22: /DRV driver for motor1/GLC -> /Sheet5F71C92D/GLC
- Q6 pad 3: /DRV driver for motor1/MOTOR_CH3 -> /Sheet5F71C92D/MOTOR_CH3
- Q6 pad 4: /DRV driver for motor1/MOTOR_CH3 -> /Sheet5F71C92D/MOTOR_CH3
- Q6 pad 5: /DRV driver for motor1/MOTOR_CH3 -> /Sheet5F71C92D/MOTOR_CH3
- Q6 pad 6: /DRV driver for motor1/MOTOR_CH3 -> /Sheet5F71C92D/MOTOR_CH3
- Q6 pad 7: /DRV driver for motor1/MOTOR_CH3 -> /Sheet5F71C92D/MOTOR_CH3
- Q6 pad 8: /DRV driver for motor1/MOTOR_CH3 -> /Sheet5F71C92D/MOTOR_CH3
- Q6 pad 9: /DRV driver for motor1/MOTOR_CH3 -> /Sheet5F71C92D/MOTOR_CH3
- R1 pad 1: /F2838x GPIOs/ANALOG_IN2 -> /sheet5F597565/ANALOG_IN2
- R10 pad 1: /F2838x GPIOs/M2_Ib -> /Power distribution/Sheet5F5C0182/REF_3V0
- R10 pad 2: Net-(R10-Pad2) -> Net-(C28-Pad1)
- R11 pad 1: /F2838x GPIOs/M2_Ia -> REF_3V0_BUF
- R11 pad 2: Net-(R11-Pad2) -> Net-(C30-Pad1)
- R12 pad 1: GND -> REF_3V0_BUF
- R12 pad 2: /DRV driver for motor2/SNB -> Net-(C31-Pad1)
- R13 pad 1: /F2838x GPIOs/M2_Vb -> VDD_1V2
- R14 pad 1: /F2838x GPIOs/~DRV2_GPIO_FAULTn~ -> 5V0
- R14 pad 2: Net-(D2-Pad1) -> /sheet5F5A100E/ENC1_A
- R15 pad 1: /F2838x GPIOs/~DRV2_GPIO_FAULTn~ -> 5V0
- R15 pad 2: VDD_3V3 -> /sheet5F5A100E/ENC1_B
- R16 pad 1: /DRV driver for motor2/MOTOR_CH3 -> 5V0
- R16 pad 2: /F2838x GPIOs/M2_Vc -> /sheet5F5A100E/ENC1_I
- R17 pad 1: GND -> 5V0
- R17 pad 2: /DRV driver for motor2/SNC -> /sheet5F5A100E/ENC2_A
- R18 pad 1: /F2838x GPIOs/M2_Vc -> 5V0
- R18 pad 2: GND -> /sheet5F5A100E/ENC2_B
- R19 pad 1: /DRV driver for motor1/MOTOR_CH1 -> 5V0
- R19 pad 2: /F2838x GPIOs/M1_Va -> /sheet5F5A100E/ENC2_I
- R2 pad 1: VPOWER -> /sheet5F597565/ANALOG_IN1
- R2 pad 2: /F2838x GPIOs/M1_Vbus -> Net-(J4-Pad2)
- R20 pad 1: GND -> VDD_3V3
- R20 pad 2: /DRV driver for motor1/SNA -> Net-(R20-Pad2)
- R21 pad 1: /F2838x GPIOs/M1_Va -> /sheet5F5B5755/CAN_H
- R21 pad 2: GND -> /sheet5F5B5755/CAN_L
- R22 pad 1: /F2838x GPIOs/M1_Ic -> /sheet5F5B5756/RX_CLK_LVDS_P
- R22 pad 2: Net-(R22-Pad2) -> /sheet5F5B5756/RX_CLK_LVDS_N
- R23 pad 1: /DRV driver for motor1/MOTOR_CH2 -> /sheet5F5B5756/RX_D0_LVDS_P
- R23 pad 2: /F2838x GPIOs/M1_Vb -> /sheet5F5B5756/RX_D0_LVDS_N
- R24 pad 1: /F2838x GPIOs/M1_Ib -> /sheet5F5B5756/RX_D1_LVDS_P
- R24 pad 2: Net-(R24-Pad2) -> /sheet5F5B5756/RX_D1_LVDS_N
- R25 pad 1: /F2838x GPIOs/M1_Ia -> GND
- R25 pad 2: Net-(R25-Pad2) -> /sheet5F597565/FSI_RXA_CLK
- R26 pad 2: /DRV driver for motor1/SNB -> /sheet5F597565/FSI_RXA_D0
- R27 pad 1: /F2838x GPIOs/M1_Vb -> GND
- R27 pad 2: GND -> /sheet5F597565/FSI_RXA_D1
- R28 pad 1: /F2838x GPIOs/~DRV1_GPIO_FAULTn~ -> Net-(R28-Pad1)
- R28 pad 2: Net-(D3-Pad1) -> GND
- R29 pad 1: /F2838x GPIOs/~DRV1_GPIO_FAULTn~ -> VDD_3V3
- R29 pad 2: VDD_3V3 -> /JTAG + CLOCK + RESET/~XRSn~
- R3 pad 1: /F2838x GPIOs/ANALOG_IN1 -> 5V0
- R3 pad 2: Net-(J5-Pad2) -> /Power distribution/Sheet5F5BD907/PG_5V0
- R30 pad 1: /DRV driver for motor1/MOTOR_CH3 -> /JTAG + CLOCK + RESET/~TRSTn~
- R30 pad 2: /F2838x GPIOs/M1_Vc -> GND
- R31 pad 2: /DRV driver for motor1/SNC -> /sheet5F597565/FSI_TXA_D0
- R32 pad 1: /F2838x GPIOs/M1_Vc -> GND
- R32 pad 2: GND -> /sheet5F597565/FSI_TXA_D1
- R33 pad 1: 5V0 -> GND
- R33 pad 2: /Power distribution/PG_5V0 -> /sheet5F597565/FSI_TXA_CLK
- R34 pad 1: Net-(D4-Pad1) -> /Sheet5F71C5AE/MOTOR_CH1
- R34 pad 2: GND -> /sheet5F597565/M1_Va
- R35 pad 1: /Power distribution/3V3 -> GND
- R35 pad 2: /Power distribution/FB_3V3 -> /Sheet5F71C5AE/SNA
- R36 pad 1: /Power distribution/FB_3V3 -> /sheet5F597565/M1_Va
- R37 pad 1: Net-(D5-Pad1) -> /sheet5F597565/M1_Ic
- R37 pad 2: GND -> Net-(R37-Pad2)
- R38 pad 1: /Power distribution/1V2 -> /Sheet5F71C5AE/MOTOR_CH2
- R38 pad 2: /Power distribution/FB_1V2 -> /sheet5F597565/M1_Vb
- R39 pad 1: /Power distribution/FB_1V2 -> /Sheet5F71C5AE/MOTOR_CH3
- R39 pad 2: GND -> /sheet5F597565/M1_Vc
- R4 pad 1: /F2838x GPIOs/M1_Vbus -> Net-(D1-Pad1)
- R40 pad 1: VDD_1V2 -> /sheet5F597565/M1_Ib
- R40 pad 2: GND -> Net-(R40-Pad2)
- R41 pad 1: 5V0 -> /sheet5F597565/M1_Ia
- R41 pad 2: /Quadrature Encoders for motor 1 & 2/ENC1_A -> Net-(R41-Pad2)
- R42 pad 1: 5V0 -> GND
- R42 pad 2: /Quadrature Encoders for motor 1 & 2/ENC1_B -> /Sheet5F71C5AE/SNB
- R43 pad 1: 5V0 -> /sheet5F597565/M1_Vb
- R43 pad 2: /Quadrature Encoders for motor 1 & 2/ENC1_I -> GND
- R44 pad 1: 5V0 -> GND
- R44 pad 2: /Quadrature Encoders for motor 1 & 2/ENC2_A -> /Sheet5F71C5AE/SNC
- R45 pad 1: 5V0 -> /sheet5F597565/M1_Vc
- R45 pad 2: /Quadrature Encoders for motor 1 & 2/ENC2_B -> GND
- R46 pad 1: 5V0 -> /sheet5F597565/~DRV1_GPIO_FAULTn~
- R46 pad 2: /Quadrature Encoders for motor 1 & 2/ENC2_I -> Net-(D3-Pad1)
- R47 pad 1: VDD_3V3 -> /sheet5F597565/~DRV1_GPIO_FAULTn~
- R47 pad 2: Net-(R47-Pad2) -> VDD_3V3
- R48 pad 1: /CAN Bus link/CAN_H -> /Sheet5F71C92D/MOTOR_CH1
- R48 pad 2: /CAN Bus link/CAN_L -> /sheet5F597565/M2_Va
- R49 pad 1: Net-(R49-Pad1) -> GND
- R49 pad 2: GND -> /Sheet5F71C92D/SNA
- R5 pad 1: /DRV driver for motor2/MOTOR_CH1 -> /Power distribution/Sheet5F5BE68A/3V3
- R5 pad 2: /F2838x GPIOs/M2_Va -> /Power distribution/Sheet5F5BE68A/FB_3V3
- R50 pad 1: VDD_3V3 -> /sheet5F597565/M2_Va
- R50 pad 2: /JTAG Bus + Oscillator + Reset/~XRSn~ -> GND
- R51 pad 1: /JTAG Bus + Oscillator + Reset/~TRSTn~ -> /sheet5F597565/M2_Ic
- R51 pad 2: GND -> Net-(R51-Pad2)
- R52 pad 1: /FSI Rx Bus Link/RX_CLK_LVDS_P -> /Sheet5F71C92D/MOTOR_CH2
- R52 pad 2: /FSI Rx Bus Link/RX_CLK_LVDS_N -> /sheet5F597565/M2_Vb
- R53 pad 1: /FSI Rx Bus Link/RX_D0_LVDS_P -> /Sheet5F71C92D/MOTOR_CH3
- R53 pad 2: /FSI Rx Bus Link/RX_D0_LVDS_N -> /sheet5F597565/M2_Vc
- R54 pad 1: /FSI Rx Bus Link/RX_D1_LVDS_P -> /sheet5F597565/M2_Ib
- R54 pad 2: /FSI Rx Bus Link/RX_D1_LVDS_N -> Net-(R54-Pad2)
- R55 pad 1: GND -> /sheet5F597565/M2_Ia
- R55 pad 2: /F2838x GPIOs/FSI_RXA_CLK -> Net-(R55-Pad2)
- R56 pad 2: /F2838x GPIOs/FSI_RXA_D0 -> /Sheet5F71C92D/SNB
- R57 pad 1: GND -> /sheet5F597565/M2_Vb
- R57 pad 2: /F2838x GPIOs/FSI_RXA_D1 -> GND
- R58 pad 1: REF_3V0_BUF -> Net-(Q6-Pad12)
- R58 pad 2: Net-(C113-Pad1) -> /Sheet5F71C92D/SPC
- R59 pad 1: REF_3V0_BUF -> /sheet5F597565/M2_Vc
- R59 pad 2: Net-(C114-Pad1) -> GND
- R6 pad 1: GND -> /Power distribution/Sheet5F5BE68A/FB_3V3
- R6 pad 2: /DRV driver for motor2/SNA -> GND
- R60 pad 1: GND -> /sheet5F597565/~DRV2_GPIO_FAULTn~
- R60 pad 2: /F2838x GPIOs/FSI_TXA_D0 -> Net-(D4-Pad1)
- R61 pad 1: GND -> /sheet5F597565/~DRV2_GPIO_FAULTn~
- R61 pad 2: /F2838x GPIOs/FSI_TXA_D1 -> VDD_3V3
- R62 pad 1: GND -> VPOWER
- R62 pad 2: /F2838x GPIOs/FSI_TXA_CLK -> /sheet5F597565/M1_Vbus
- R7 pad 1: /F2838x GPIOs/M2_Va -> Net-(D2-Pad1)
- R8 pad 1: /F2838x GPIOs/M2_Ic -> /Power distribution/Sheet5F5BF411/1V2
- R8 pad 2: Net-(R8-Pad2) -> /Power distribution/Sheet5F5BF411/FB_1V2
- R9 pad 1: /DRV driver for motor2/MOTOR_CH2 -> /Power distribution/Sheet5F5BF411/FB_1V2
- R9 pad 2: /F2838x GPIOs/M2_Vb -> GND
- SW1 pad 2: /JTAG Bus + Oscillator + Reset/~XRSn~ -> /JTAG + CLOCK + RESET/~XRSn~
- TP1 pad 1: VPOWER -> GND
- TP10 pad 1: /DRV driver for motor2/GHC -> /Sheet5F71C5AE/GHA
- TP11 pad 1: /DRV driver for motor2/GLC -> Net-(C74-Pad2)
- TP12 pad 1: /F2838x GPIOs/M2_Vc -> /Sheet5F71C5AE/GLA
- TP13 pad 1: /DRV driver for motor1/GHA -> /sheet5F597565/M1_Va
- TP14 pad 1: Net-(C27-Pad2) -> /Sheet5F71C5AE/GHB
- TP15 pad 1: /DRV driver for motor1/GLA -> /Sheet5F71C5AE/GHC
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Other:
- board outline added: 50 x 50 mm
